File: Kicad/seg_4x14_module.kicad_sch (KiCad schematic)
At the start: 1 part, among them U2 HT16K33A-28SSOP

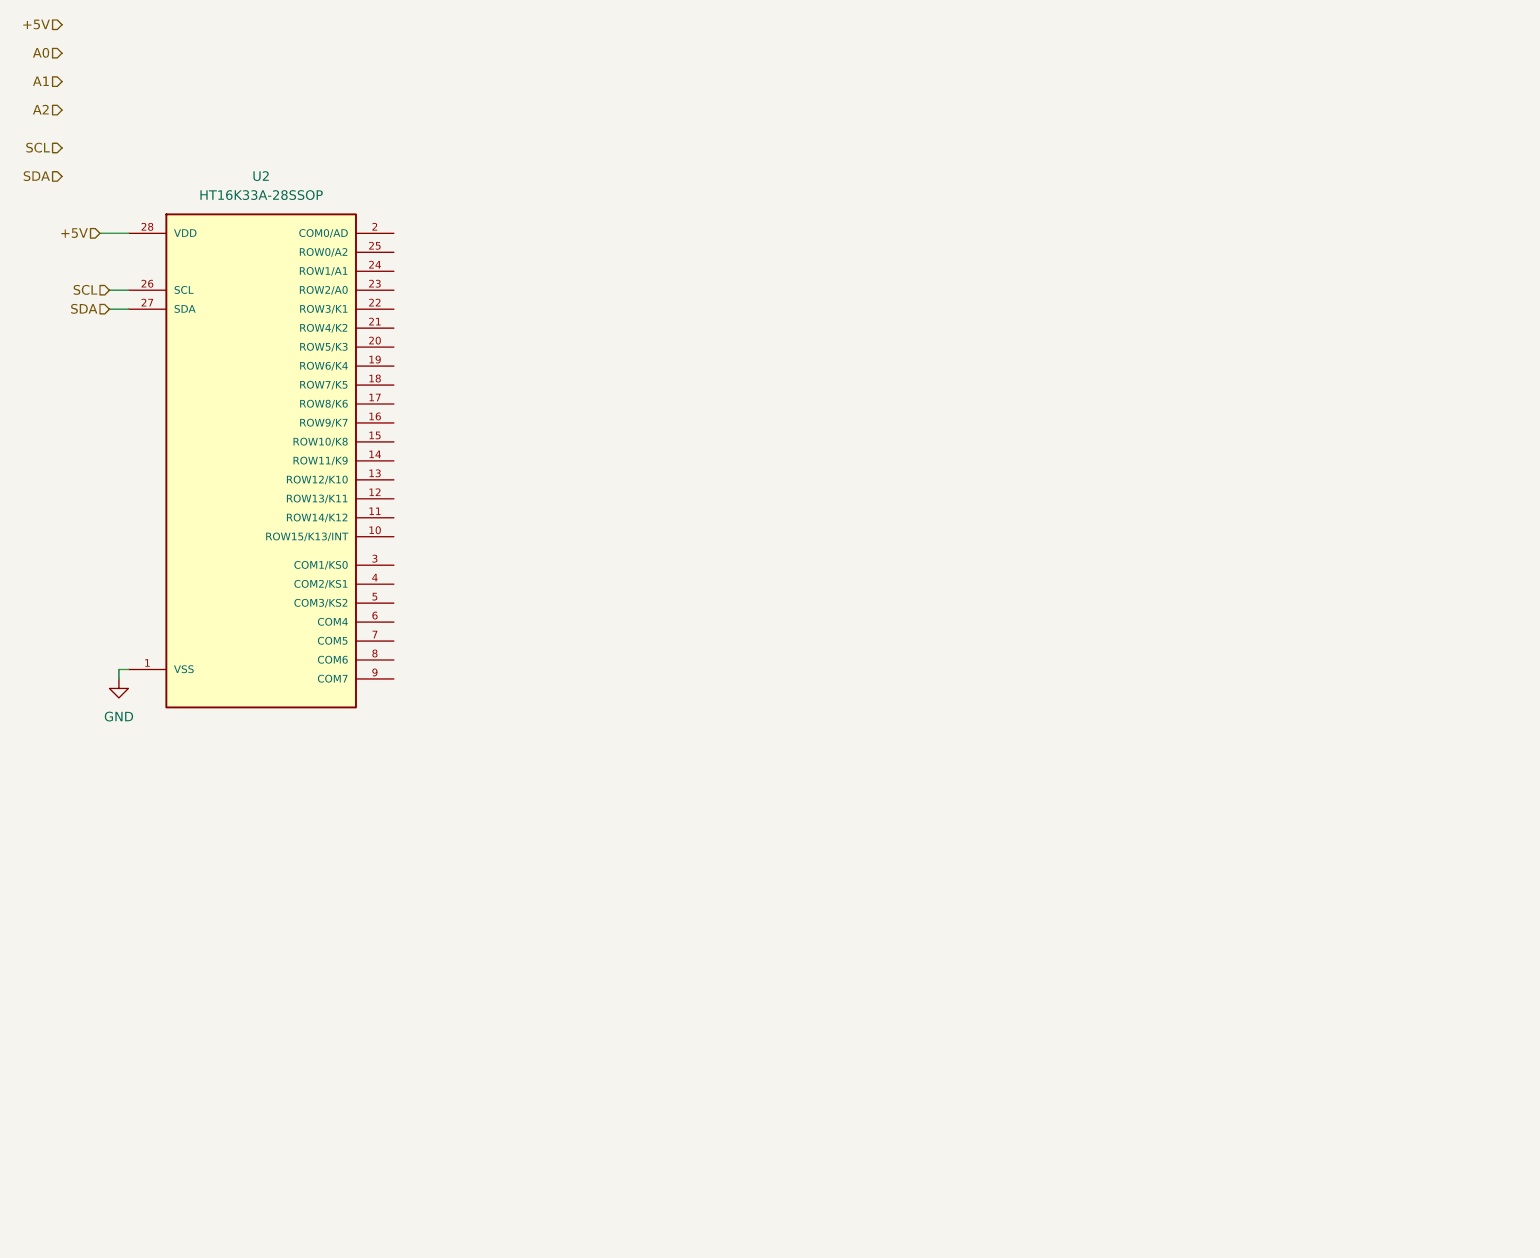
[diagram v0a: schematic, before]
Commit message: adding multiple component (14 semgent and led)
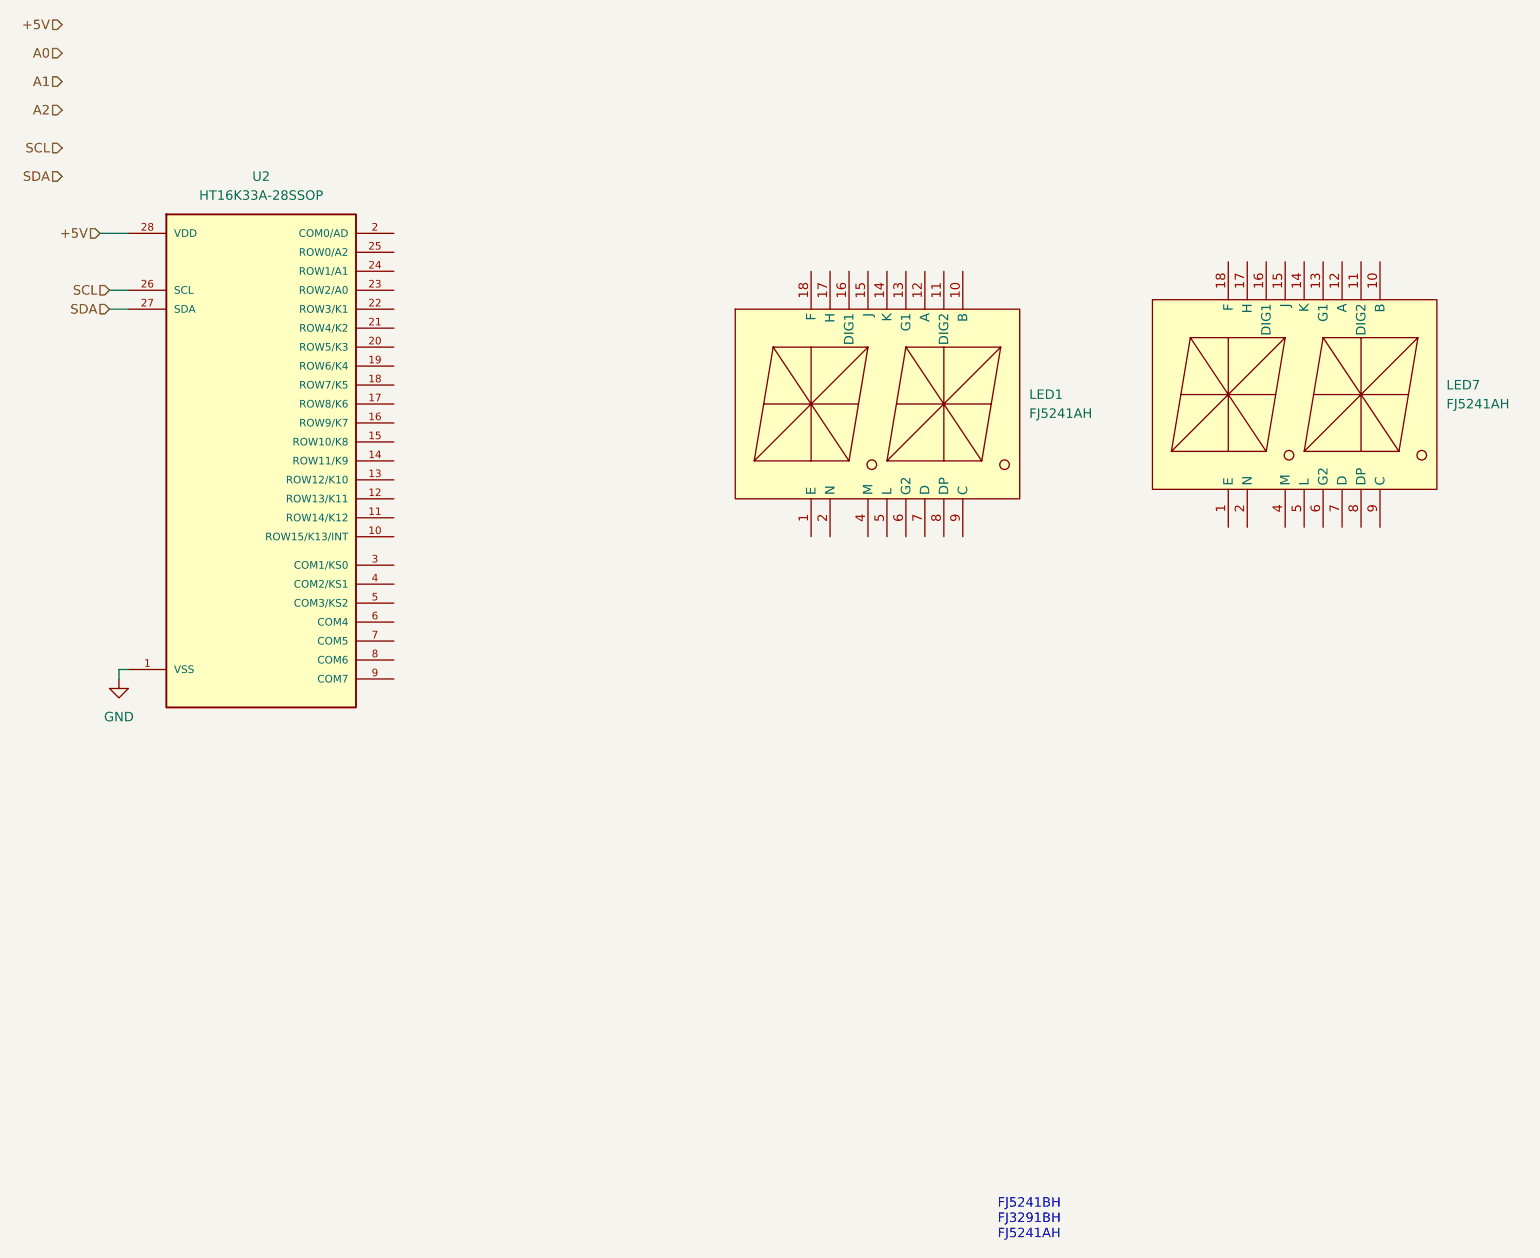
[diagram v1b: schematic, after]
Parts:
- added LED1, LED7: FJ5241AH, Eeloo_Pad:LED-SEG-TH_18P-L25.2-W21.1-P2.54-LS15.2-BL, symbol Eeloo_Pad:FJ5241AH
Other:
- note added: "FJ5241BHr FJ3291BHr FJ5241AH"

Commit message: working on the 14 segment schematics
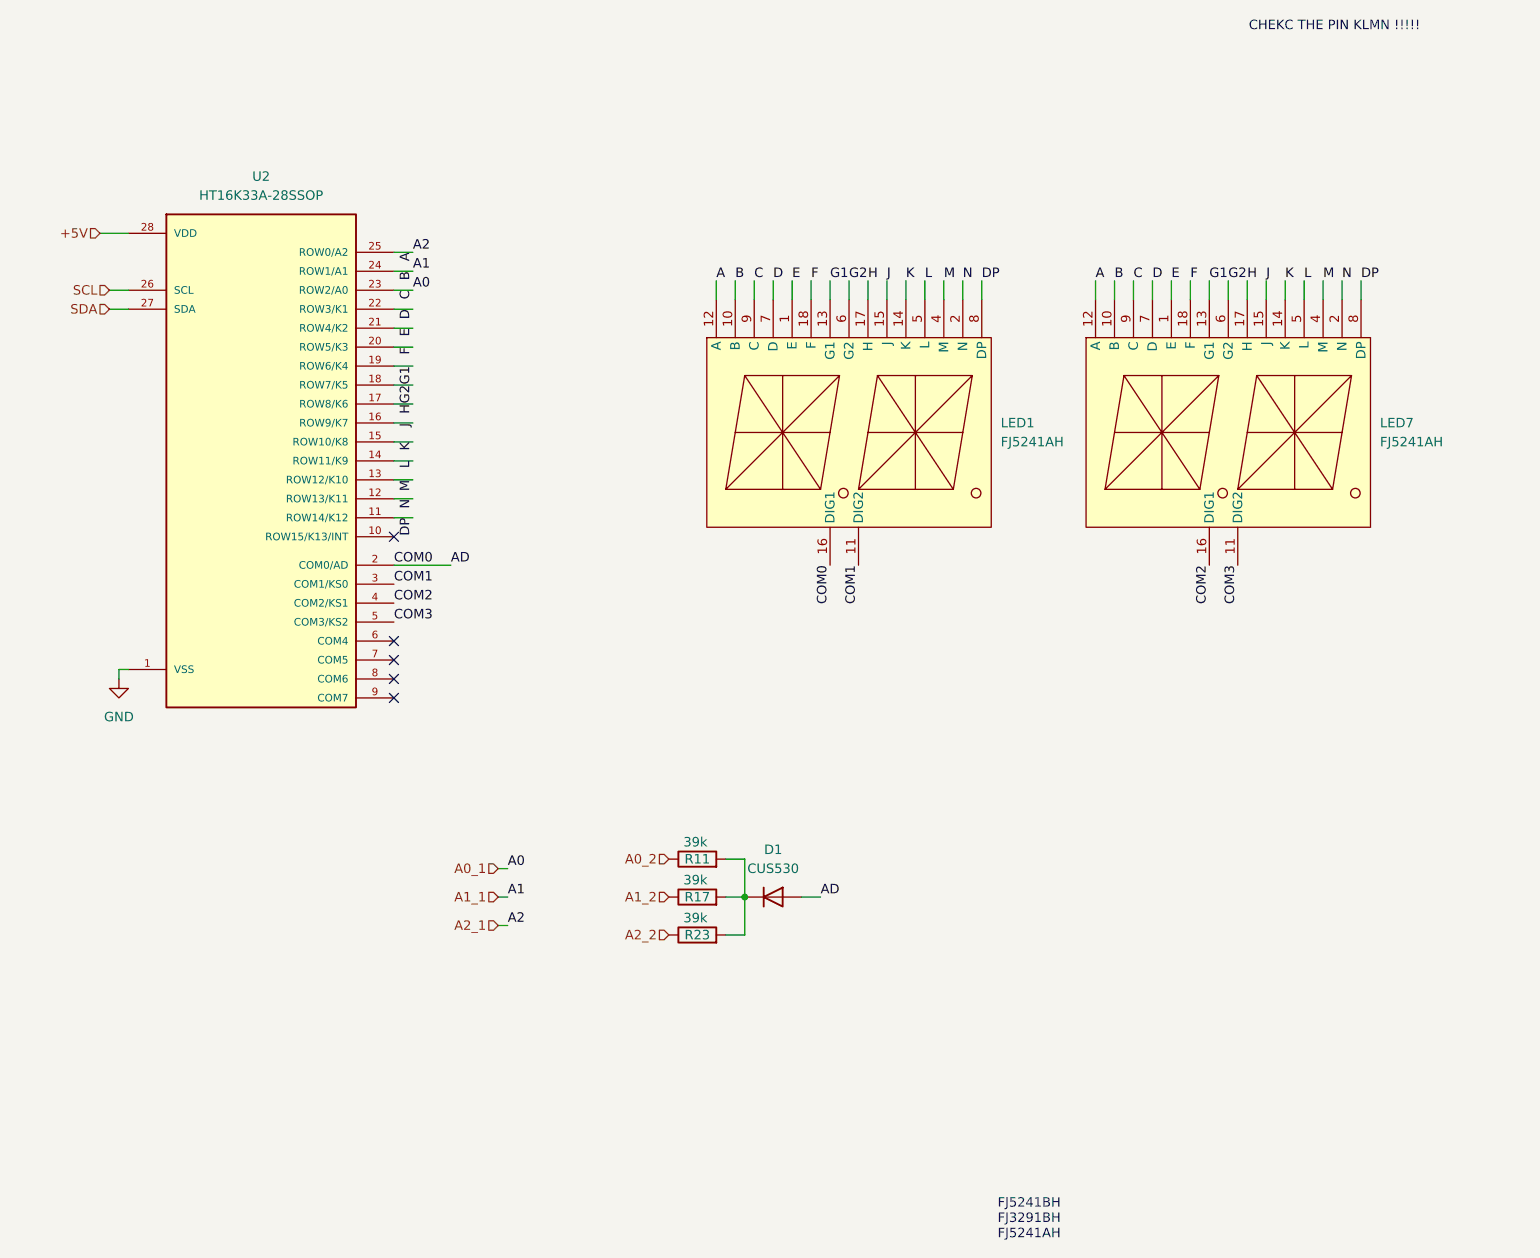
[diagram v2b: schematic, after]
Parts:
- added D1: CUS530, symbol Device:D
- added R11, R17, R23: 39k, symbol Device:R
- LED1, LED7: footprint Eeloo_Pad:LED-SEG-TH_18P-L25.2-W21.1-P2.54-LS15.2-BL -> 4segment_x2:LED-SEG-TH_18P-L25.2-W21.1-P2.54-LS15.2-BL
- U2: footprint Eeloo_Pad:SOP63P600X175-28N -> HT16K33A-28SSOP:SOP63P600X175-28N
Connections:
- net E: now reaches LED1.1 (E)
- net E: now also LED7.1 (E), U2.21 (ROW4/K2)
- net A1_1: now reaches LED1.10 (B)
- net A1_1: now also LED7.10 (B), U2.24 (ROW1/A1)
- net COM1: now reaches LED1.11 (DIG2)
- net COM1: now also U2.3 (COM1/KS0)
- net A2_1: now reaches LED1.12 (A)
- net A2_1: now also LED7.12 (A), U2.25 (ROW0/A2)
- net G1: now reaches LED1.13 (G1)
- net G1: now also LED7.13 (G1), U2.19 (ROW6/K4)
- net K: now reaches LED1.14 (K)
- net K: now also LED7.14 (K), U2.15 (ROW10/K8)
- net J: now reaches LED1.15 (J)
- net J: now also LED7.15 (J), U2.16 (ROW9/K7)
- net AD: now reaches LED1.16 (DIG1)
- net AD: now also U2.2 (COM0/AD), D1.2 (A)
- net H: now reaches LED1.17 (H)
- net H: now also LED7.17 (H), U2.17 (ROW8/K6)
- net F: now reaches LED1.18 (F)
- net F: now also LED7.18 (F), U2.20 (ROW5/K3)
- net N: now reaches LED1.2 (N)
- net N: now also LED7.2 (N), U2.12 (ROW13/K11)
- net M: now reaches LED1.4 (M)
- net M: now also LED7.4 (M), U2.13 (ROW12/K10)
- net L: now reaches LED1.5 (L)
- net L: now also LED7.5 (L), U2.14 (ROW11/K9)
- net G2: now reaches LED1.6 (G2)
- net G2: now also LED7.6 (G2), U2.18 (ROW7/K5)
- net D: now reaches LED1.7 (D)
- net D: now also LED7.7 (D), U2.22 (ROW3/K1)
- net DP: now reaches LED1.8 (DP)
- net DP: now also LED7.8 (DP), U2.11 (ROW14/K12)
- net A0_1: now reaches LED1.9 (C)
- net A0_1: now also LED7.9 (C), U2.23 (ROW2/A0)
- net COM3: now reaches LED7.11 (DIG2)
- net COM3: now also U2.5 (COM3/KS2)
- net COM2: now reaches LED7.16 (DIG1)
- net COM2: now also U2.4 (COM2/KS1)
- new net: D1.1 (K), R11.2, R17.2, R23.2
- new net A0_2: R11.1
- new net A1_2: R17.1
- new net A2_2: R23.1
- no-connect marks 0 -> 5
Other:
- note added: "CHEKC THE PIN KLMN !!!!!"
- moved on the sheet: LED1, LED7
